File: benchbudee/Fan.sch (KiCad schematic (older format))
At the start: 0 parts

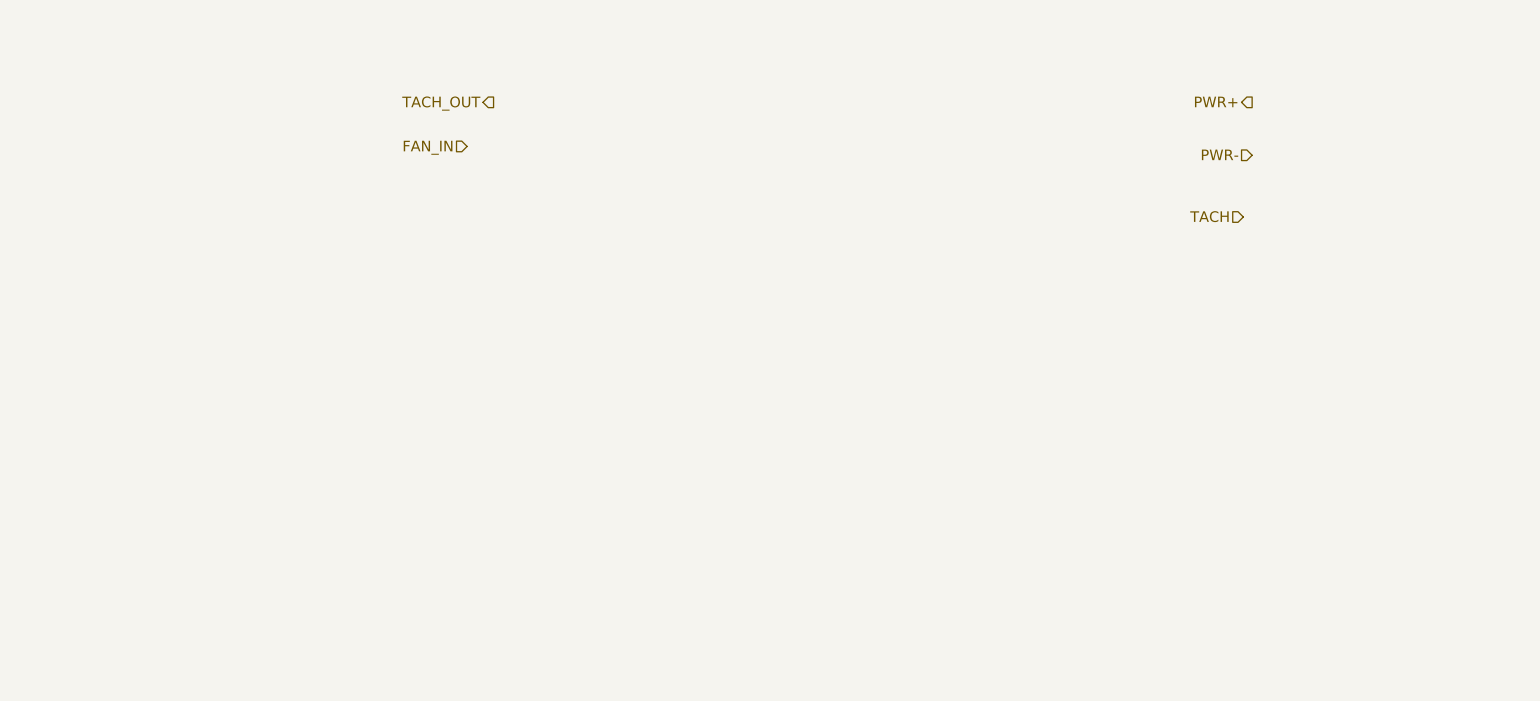
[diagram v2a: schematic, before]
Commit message: Added first crack at fan module
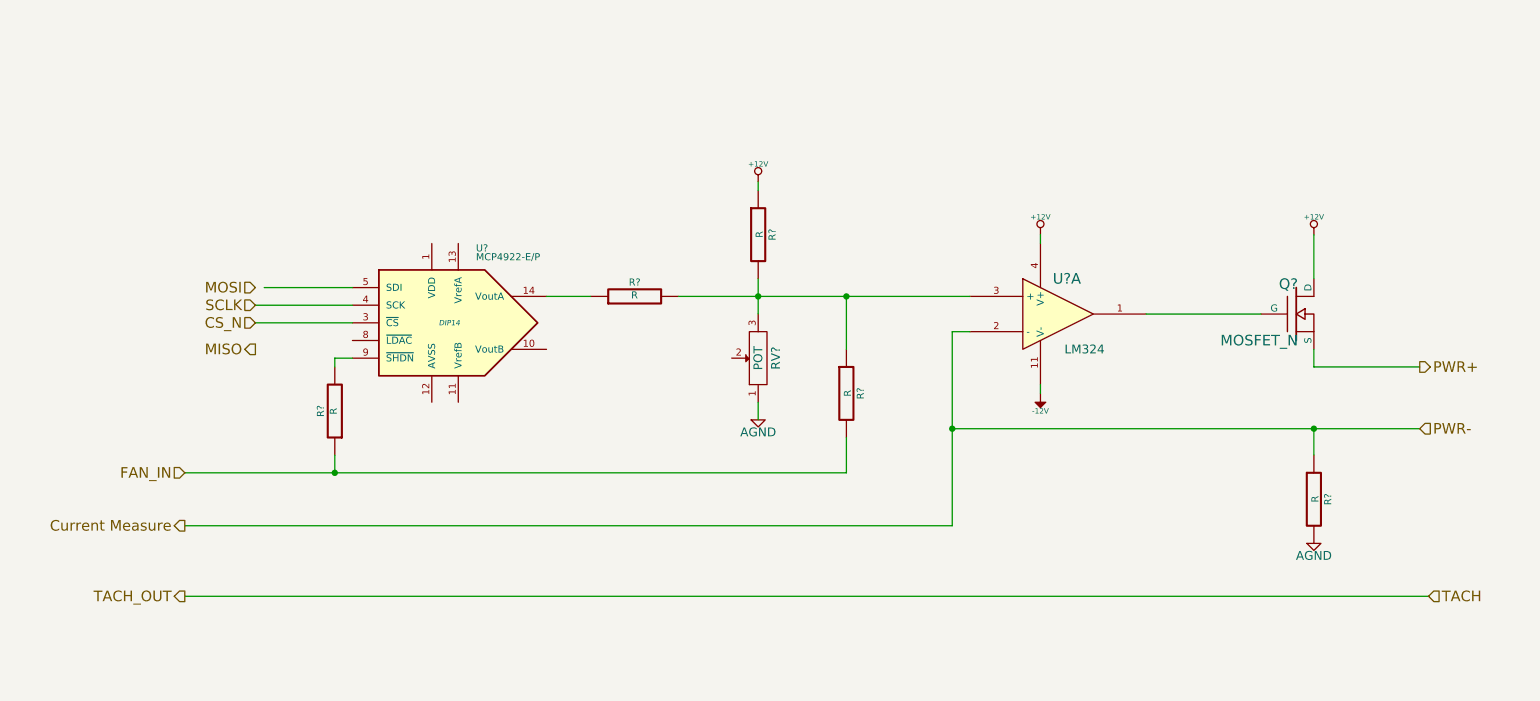
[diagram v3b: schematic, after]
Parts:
- added Q?: MOSFET_N, ~, symbol MOSFET_N
- added R? (x5): R, ~, symbol R
- added RV?: POT, ~, symbol POT
- added U?: LM324, symbol LM324
- added U?: MCP4922-E/P, DIP14, symbol MCP4922-E/P
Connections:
- net labels added: +12V, -12V, AGND, CS_N, Current Measure, MISO, MOSI, SCLK
- wire segments 0 -> 32

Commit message: Setting up for layout
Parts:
- removed R? (x4): R, ~, symbol R
- removed RV?: POT, ~, symbol POT
- added D?: DIODE, symbol DIODE
- added Q? (x2): MOSFET_N, ~, symbol MOSFET_N
- added R?: R, symbol R
- added TH?: THERMISTOR, symbol THERMISTOR
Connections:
- net labels added: +12C, CURR_MEAS, FAN_MODE, FAN_OUT+, FAN_OUT-, FAN_PWM, TACH_IN, TACH_MEAS
- net labels removed: Current Measure, FAN_IN, PWR+, PWR-, TACH, TACH_OUT
- wire segments 32 -> 34
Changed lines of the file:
@@
 LIBS:benchbudee-custom
 LIBS:benchbudee-cache
-EELAYER 27 0
+EELAYER 24 0
 EELAYER END
 $Descr A4 11693 8268
@@
 Comment4 ""
 $EndDescr
-Text HLabel 9350 3150 2    60   Output ~ 0
-PWR+
-Text HLabel 9350 3500 2    60   Input ~ 0
-PWR-
-Text HLabel 9400 4450 2    60   Input ~ 0
-TACH
-Text HLabel 2350 4450 0    60   Output ~ 0
-TACH_OUT
-Text HLabel 2350 3750 0    60   Input ~ 0
-FAN_IN
+Text HLabel 9350 2050 2    60   Output ~ 0
+FAN_OUT+
+Text HLabel 9350 2450 2    60   Output ~ 0
+FAN_OUT-
+Text HLabel 9400 4900 2    60   Input ~ 0
+TACH_IN
+Text HLabel 2350 4900 0    60   Output ~ 0
+TACH_MEAS
+Text HLabel 2350 3450 0    60   Input ~ 0
+FAN_PWM
 $Comp
 L LM324 U?
@@
 F 3 "~" H 8650 2850 60  0000 C CNN
 	1    8650 2850
-	1    0    0    -1
-$EndComp
-$Comp
-L +12V #PWR?
-U 1 1 52FBCD3F
-P 8750 2400
-F 0 "#PWR?" H 8750 2350 20  0001 C CNN
-F 1 "+12V" H 8750 2500 30  0000 C CNN
-F 2 "" H 8750 2400 60  0000 C CNN
-F 3 "" H 8750 2400 60  0000 C CNN
-	1    8750 2400
-	1    0    0    -1
-$EndComp
-$Comp
-L R R?
-U 1 1 52FBCD6B
-P 8750 3900
-F 0 "R?" V 8830 3900 40  0000 C CNN
-F 1 "R" V 8757 3901 40  0000 C CNN
-F 2 "~" V 8680 3900 30  0000 C CNN
-F 3 "~" H 8750 3900 30  0000 C CNN
-	1    8750 3900
-	1    0    0    -1
-$EndComp
-$Comp
-L AGND #PWR?
-U 1 1 52FBCD84
-P 8750 4150
-F 0 "#PWR?" H 8750 4150 40  0001 C CNN
-F 1 "AGND" H 8750 4080 50  0000 C CNN
-F 2 "" H 8750 4150 60  0000 C CNN
-F 3 "" H 8750 4150 60  0000 C CNN
-	1    8750 4150
 	1    0    0    -1
 $EndComp
@@
 $EndComp
 $Comp
-L R R?
-U 1 1 52FBCDEF
-P 5600 2400
-F 0 "R?" V 5680 2400 40  0000 C CNN
-F 1 "R" V 5607 2401 40  0000 C CNN
-F 2 "~" V 5530 2400 30  0000 C CNN
-F 3 "~" H 5600 2400 30  0000 C CNN
-	1    5600 2400
-	1    0    0    -1
-$EndComp
-$Comp
-L +12V #PWR?
-U 1 1 52FBCDFC
-P 5600 2100
-F 0 "#PWR?" H 5600 2050 20  0001 C CNN
-F 1 "+12V" H 5600 2200 30  0000 C CNN
-F 2 "" H 5600 2100 60  0000 C CNN
-F 3 "" H 5600 2100 60  0000 C CNN
-	1    5600 2100
-	1    0    0    -1
-$EndComp
-$Comp
-L POT RV?
-U 1 1 52FBCE11
-P 5600 3100
-F 0 "RV?" H 5600 3000 50  0000 C CNN
-F 1 "POT" H 5600 3100 50  0000 C CNN
-F 2 "~" H 5600 3100 60  0000 C CNN
-F 3 "~" H 5600 3100 60  0000 C CNN
-	1    5600 3100
-	0    -1   -1   0
-$EndComp
-$Comp
-L AGND #PWR?
-U 1 1 52FBCE3B
-P 5600 3450
-F 0 "#PWR?" H 5600 3450 40  0001 C CNN
-F 1 "AGND" H 5600 3380 50  0000 C CNN
-F 2 "" H 5600 3450 60  0000 C CNN
-F 3 "" H 5600 3450 60  0000 C CNN
-	1    5600 3450
-	1    0    0    -1
-$EndComp
-$Comp
 L MCP4922-E/P U?
 U 1 1 52FBCE6B
@@
 	1    0    0    -1
 $EndComp
-Text HLabel 2350 4050 0    60   Output ~ 0
-Current Measure
-$Comp
-L R R?
-U 1 1 52FBCF59
-P 6100 3300
-F 0 "R?" V 6180 3300 40  0000 C CNN
-F 1 "R" V 6107 3301 40  0000 C CNN
-F 2 "~" V 6030 3300 30  0000 C CNN
-F 3 "~" H 6100 3300 30  0000 C CNN
-	1    6100 3300
-	1    0    0    -1
-$EndComp
+Text HLabel 2350 3750 0    60   Output ~ 0
+CURR_MEAS
 $Comp
 L R R?
@@
 SCLK
 $Comp
+L THERMISTOR TH?
+U 1 1 532606F8
+P 8750 1650
+F 0 "TH?" V 8850 1700 50  0000 C CNN
+F 1 "THERMISTOR" V 8650 1650 50  0000 C CNN
+F 2 "" H 8750 1650 60  0000 C CNN
+F 3 "" H 8750 1650 60  0000 C CNN
+	1    8750 1650
+	1    0    0    -1
+$EndComp
+Wire Wire Line
+	7800 2850 8450 2850
+Wire Wire Line
+	6700 2950 6800 2950
+Wire Wire Line
+	7200 2400 7200 2450
+Wire Wire Line
+	7200 3300 7200 3250
+Wire Wire Line
+	2350 4900 9400 4900
+Wire Wire Line
+	4400 2750 4650 2750
+Wire Wire Line
+	5400 3100 5400 3450
+Wire Wire Line
+	5400 3450 2350 3450
+Wire Wire Line
+	2800 2700 3300 2700
+Wire Wire Line
+	2750 2800 3300 2800
+Wire Wire Line
+	2750 2900 3300 2900
+Wire Wire Line
+	8750 1300 8750 1400
+Wire Wire Line
+	8750 1900 8750 2050
+Wire Wire Line
+	8500 2050 8750 2050
+Wire Wire Line
+	8750 2050 9350 2050
+Wire Wire Line
+	8500 2450 8750 2450
+Wire Wire Line
+	8750 2450 9350 2450
+Wire Wire Line
+	8750 2450 8750 2650
+$Comp
+L DIODE D?
+U 1 1 532607DB
+P 8500 2250
+F 0 "D?" H 8500 2350 40  0000 C CNN
+F 1 "DIODE" H 8500 2150 40  0000 C CNN
+F 2 "" H 8500 2250 60  0000 C CNN
+F 3 "" H 8500 2250 60  0000 C CNN
+	1    8500 2250
+	0    -1   -1   0
+$EndComp
+Connection ~ 8750 2050
+Connection ~ 8750 2450
+Wire Wire Line
+	8750 3050 8750 3750
+Wire Wire Line
+	8750 3750 8750 4000
+$Comp
+L MOSFET_N Q?
+U 1 1 532608A6
+P 8050 4250
+F 0 "Q?" H 8060 4420 60  0000 R CNN
+F 1 "MOSFET_N" H 8060 4100 60  0000 R CNN
+F 2 "~" H 8050 4250 60  0000 C CNN
+F 3 "~" H 8050 4250 60  0000 C CNN
+	1    8050 4250
+	1    0    0    -1
+$EndComp
+$Comp
 L R R?
-U 1 1 52FBD047
-P 3200 3400
-F 0 "R?" V 3280 3400 40  0000 C CNN
-F 1 "R" V 3207 3401 40  0000 C CNN
-F 2 "~" V 3130 3400 30  0000 C CNN
-F 3 "~" H 3200 3400 30  0000 C CNN
-	1    3200 3400
-	-1   0    0    1
-$EndComp
-Wire Wire Line
-	7800 2850 8450 2850
-Wire Wire Line
-	8750 2400 8750 2650
-Wire Wire Line
-	8750 3050 8750 3150
-Wire Wire Line
-	8750 3150 9350 3150
-Wire Wire Line
-	6700 3500 8750 3500
-Wire Wire Line
-	8750 3500 9350 3500
-Wire Wire Line
-	8750 3500 8750 3650
-Wire Wire Line
-	6700 2950 6700 3500
-Wire Wire Line
-	6700 3500 6700 4050
-Wire Wire Line
-	6700 2950 6800 2950
-Connection ~ 8750 3500
-Wire Wire Line
-	7200 2400 7200 2450
-Wire Wire Line
-	7200 3300 7200 3250
-Wire Wire Line
-	5600 2100 5600 2150
-Wire Wire Line
-	5600 2650 5600 2750
-Wire Wire Line
-	5600 2750 5600 2850
-Wire Wire Line
-	5150 2750 5600 2750
-Wire Wire Line
-	5600 2750 6100 2750
-Wire Wire Line
-	6100 2750 6800 2750
-Connection ~ 5600 2750
-Wire Wire Line
-	5600 3350 5600 3450
-Wire Wire Line
-	6700 4050 2350 4050
-Connection ~ 6700 3500
-Wire Wire Line
-	2350 4450 9400 4450
-Wire Wire Line
-	4400 2750 4650 2750
-Wire Wire Line
-	6100 3050 6100 2750
-Connection ~ 6100 2750
-Wire Wire Line
-	6100 3550 6100 3750
-Wire Wire Line
-	6100 3750 3200 3750
-Wire Wire Line
-	3200 3750 2350 3750
-Wire Wire Line
-	2800 2700 3300 2700
-Wire Wire Line
-	2750 2800 3300 2800
-Wire Wire Line
-	2750 2900 3300 2900
-Wire Wire Line
-	3200 3150 3200 3100
-Wire Wire Line
-	3200 3100 3300 3100
-Wire Wire Line
-	3200 3650 3200 3750
-Connection ~ 3200 3750
+U 1 1 532608E6
+P 8750 4250
+F 0 "R?" V 8830 4250 40  0000 C CNN
+F 1 "R" V 8757 4251 40  0000 C CNN
+F 2 "" V 8680 4250 30  0000 C CNN
+F 3 "" H 8750 4250 30  0000 C CNN
+	1    8750 4250
+	1    0    0    -1
+$EndComp
+$Comp
+L AGND #PWR?
+U 1 1 532608FA
+P 8750 4650
+F 0 "#PWR?" H 8750 4650 40  0001 C CNN
+F 1 "AGND" H 8750 4580 50  0000 C CNN
+F 2 "" H 8750 4650 60  0000 C CNN
+F 3 "" H 8750 4650 60  0000 C CNN
+	1    8750 4650
+	1    0    0    -1
+$EndComp
+Wire Wire Line
+	8750 4500 8750 4650
+Wire Wire Line
+	8150 4500 8750 4500
+Wire Wire Line
+	2350 3750 6700 3750
+Wire Wire Line
+	6700 3750 8150 3750
+Wire Wire Line
+	8150 3750 8750 3750
+Wire Wire Line
+	8150 3750 8150 4050
+Wire Wire Line
+	6700 2950 6700 3750
+Connection ~ 8150 3750
+Connection ~ 6700 3750
+Connection ~ 8750 3750
+Wire Wire Line
+	8150 4500 8150 4450
+Wire Wire Line
+	5150 2750 6150 2750
+Wire Wire Line
+	6150 2750 6800 2750
+$Comp
+L MOSFET_N Q?
+U 1 1 53260AAD
+P 6050 3100
+F 0 "Q?" H 6060 3270 60  0000 R CNN
+F 1 "MOSFET_N" H 6060 2950 60  0000 R CNN
+F 2 "~" H 6050 3100 60  0000 C CNN
+F 3 "~" H 6050 3100 60  0000 C CNN
+	1    6050 3100
+	1    0    0    -1
+$EndComp
+Wire Wire Line
+	6150 2900 6150 2750
+Connection ~ 6150 2750
+Wire Wire Line
+	5400 3100 5850 3100
+$Comp
+L AGND #PWR?
+U 1 1 53260B07
+P 6150 3400
+F 0 "#PWR?" H 6150 3400 40  0001 C CNN
+F 1 "AGND" H 6150 3330 50  0000 C CNN
+F 2 "" H 6150 3400 60  0000 C CNN
+F 3 "" H 6150 3400 60  0000 C CNN
+	1    6150 3400
+	1    0    0    -1
+$EndComp
+Wire Wire Line
+	6150 3300 6150 3400
+Wire Wire Line
+	7850 4250 2350 4250
+Text HLabel 2350 4250 0    60   Input ~ 0
+FAN_MODE
+$Comp
+L +12C #PWR?
+U 1 1 53261310
+P 8750 1300
+F 0 "#PWR?" H 8750 1270 30  0001 C CNN
+F 1 "+12C" H 8750 1410 40  0000 C CNN
+F 2 "" H 8750 1300 60  0000 C CNN
+F 3 "" H 8750 1300 60  0000 C CNN
+	1    8750 1300
+	1    0    0    -1
+$EndComp
 $EndSCHEMATC

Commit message: Relay module footprints done
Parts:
- gave numbers to parts that had none: 9
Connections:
- net CURR_MEAS: now also U10.9 (-); no longer U10.2 (-)
- net at Q4.G: now also U10.8; no longer U10.1
- net at Q2.D, R25.2: now also U10.10 (+); no longer U10.3 (+)
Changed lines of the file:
@@
 FAN_PWM
 $Comp
-L LM324 U?
-U 1 1 52FBCCEC
+L LM324 U10
+U 3 1 52FBCCEC
 P 7300 2850
-F 0 "U?" H 7350 3050 60  0000 C CNN
+F 0 "U10" H 7350 3050 60  0000 C CNN
 F 1 "LM324" H 7450 2650 50  0000 C CNN
 F 2 "" H 7300 2850 60  0000 C CNN
 F 3 "" H 7300 2850 60  0000 C CNN
-	1    7300 2850
-	1    0    0    -1
-$EndComp
-$Comp
-L MOSFET_N Q?
+	3    7300 2850
+	1    0    0    -1
+$EndComp
+$Comp
+L MOSFET_N Q4
 U 1 1 52FBCD26
 P 8650 2850
-F 0 "Q?" H 8660 3020 60  0000 R CNN
+F 0 "Q4" H 8660 3020 60  0000 R CNN
 F 1 "MOSFET_N" H 8660 2700 60  0000 R CNN
 F 2 "~" H 8650 2850 60  0000 C CNN
@@
 $EndComp
 $Comp
-L +12V #PWR?
+L +12V #PWR048
 U 1 1 52FBCDAD
 P 7200 2400
-F 0 "#PWR?" H 7200 2350 20  0001 C CNN
+F 0 "#PWR048" H 7200 2350 20  0001 C CNN
 F 1 "+12V" H 7200 2500 30  0000 C CNN
 F 2 "" H 7200 2400 60  0000 C CNN
@@
 $EndComp
 $Comp
-L -12V #PWR?
+L -12V #PWR049
 U 1 1 52FBCDD4
 P 7200 3300
-F 0 "#PWR?" H 7200 3430 20  0001 C CNN
+F 0 "#PWR049" H 7200 3430 20  0001 C CNN
 F 1 "-12V" H 7200 3400 30  0000 C CNN
 F 2 "" H 7200 3300 60  0000 C CNN
@@
 $EndComp
 $Comp
-L MCP4922-E/P U?
+L MCP4922-E/P U11
 U 1 1 52FBCE6B
 P 3850 2900
-F 0 "U?" H 4000 3300 40  0000 L BNN
+F 0 "U11" H 4000 3300 40  0000 L BNN
 F 1 "MCP4922-E/P" H 4000 3250 40  0000 L BNN
 F 2 "DIP14" H 3850 2900 30  0000 C CIN
@@
 CURR_MEAS
 $Comp
-L R R?
+L R R25
 U 1 1 52FBCF5F
 P 4900 2750
-F 0 "R?" V 4980 2750 40  0000 C CNN
+F 0 "R25" V 4980 2750 40  0000 C CNN
 F 1 "R" V 4907 2751 40  0000 C CNN
 F 2 "~" V 4830 2750 30  0000 C CNN
@@
 SCLK
 $Comp
-L THERMISTOR TH?
+L THERMISTOR TH5
 U 1 1 532606F8
 P 8750 1650
-F 0 "TH?" V 8850 1700 50  0000 C CNN
+F 0 "TH5" V 8850 1700 50  0000 C CNN
 F 1 "THERMISTOR" V 8650 1650 50  0000 C CNN
 F 2 "" H 8750 1650 60  0000 C CNN
@@
 	8750 1900 8750 2050
 Wire Wire Line
-	8500 2050 8750 2050
-Wire Wire Line
-	8750 2050 9350 2050
-Wire Wire Line
-	8500 2450 8750 2450
-Wire Wire Line
-	8750 2450 9350 2450
+	8500 2050 9350 2050
+Wire Wire Line
+	8500 2450 9350 2450
 Wire Wire Line
 	8750 2450 8750 2650
 $Comp
-L DIODE D?
+L DIODE D5
 U 1 1 532607DB
 P 8500 2250
-F 0 "D?" H 8500 2350 40  0000 C CNN
+F 0 "D5" H 8500 2350 40  0000 C CNN
 F 1 "DIODE" H 8500 2150 40  0000 C CNN
 F 2 "" H 8500 2250 60  0000 C CNN
@@
 Connection ~ 8750 2450
 Wire Wire Line
-	8750 3050 8750 3750
-Wire Wire Line
-	8750 3750 8750 4000
-$Comp
-L MOSFET_N Q?
+	8750 3050 8750 4000
+$Comp
+L MOSFET_N Q3
 U 1 1 532608A6
 P 8050 4250
-F 0 "Q?" H 8060 4420 60  0000 R CNN
+F 0 "Q3" H 8060 4420 60  0000 R CNN
 F 1 "MOSFET_N" H 8060 4100 60  0000 R CNN
 F 2 "~" H 8050 4250 60  0000 C CNN
@@
 $EndComp
 $Comp
-L R R?
+L R R26
 U 1 1 532608E6
 P 8750 4250
-F 0 "R?" V 8830 4250 40  0000 C CNN
+F 0 "R26" V 8830 4250 40  0000 C CNN
 F 1 "R" V 8757 4251 40  0000 C CNN
 F 2 "" V 8680 4250 30  0000 C CNN
@@
 $EndComp
 $Comp
-L AGND #PWR?
+L AGND #PWR050
 U 1 1 532608FA
 P 8750 4650
-F 0 "#PWR?" H 8750 4650 40  0001 C CNN
+F 0 "#PWR050" H 8750 4650 40  0001 C CNN
 F 1 "AGND" H 8750 4580 50  0000 C CNN
 F 2 "" H 8750 4650 60  0000 C CNN
@@
 	8150 4500 8750 4500
 Wire Wire Line
-	2350 3750 6700 3750
-Wire Wire Line
-	6700 3750 8150 3750
-Wire Wire Line
-	8150 3750 8750 3750
+	2350 3750 8750 3750
 Wire Wire Line
 	8150 3750 8150 4050
@@
 	8150 4500 8150 4450
 Wire Wire Line
-	5150 2750 6150 2750
-Wire Wire Line
-	6150 2750 6800 2750
-$Comp
-L MOSFET_N Q?
+	5150 2750 6800 2750
+$Comp
+L MOSFET_N Q2
 U 1 1 53260AAD
 P 6050 3100
-F 0 "Q?" H 6060 3270 60  0000 R CNN
+F 0 "Q2" H 6060 3270 60  0000 R CNN
 F 1 "MOSFET_N" H 6060 2950 60  0000 R CNN
 F 2 "~" H 6050 3100 60  0000 C CNN
@@
 	5400 3100 5850 3100
 $Comp
-L AGND #PWR?
+L AGND #PWR051
 U 1 1 53260B07
 P 6150 3400
-F 0 "#PWR?" H 6150 3400 40  0001 C CNN
+F 0 "#PWR051" H 6150 3400 40  0001 C CNN
 F 1 "AGND" H 6150 3330 50  0000 C CNN
 F 2 "" H 6150 3400 60  0000 C CNN
@@
 FAN_MODE
 $Comp
-L +12C #PWR?
+L +12C #PWR052
 U 1 1 53261310
 P 8750 1300
-F 0 "#PWR?" H 8750 1270 30  0001 C CNN
+F 0 "#PWR052" H 8750 1270 30  0001 C CNN
 F 1 "+12C" H 8750 1410 40  0000 C CNN
 F 2 "" H 8750 1300 60  0000 C CNN
